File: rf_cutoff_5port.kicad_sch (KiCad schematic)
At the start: 11 parts

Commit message: Added mode switch
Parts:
- added SW?: SW_SP3T, symbol Switch:SW_SP3T
- J?: footprint (none) -> Connector_USB:USB_C_Receptacle_Amphenol_12401548E4-2A
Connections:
- net GND: now also SW?.4
- net at C?.1, Q?.3 (D), R?.1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: now also SW?.2; no longer Q?.2 (G)
- new net: Q?.2 (G), SW?.3
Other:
- note added: "RX AUTO"
- note added: "RX OFF"
- note added: "RX ON"
- moved on the sheet: C?, D?, J?, Q?, R?

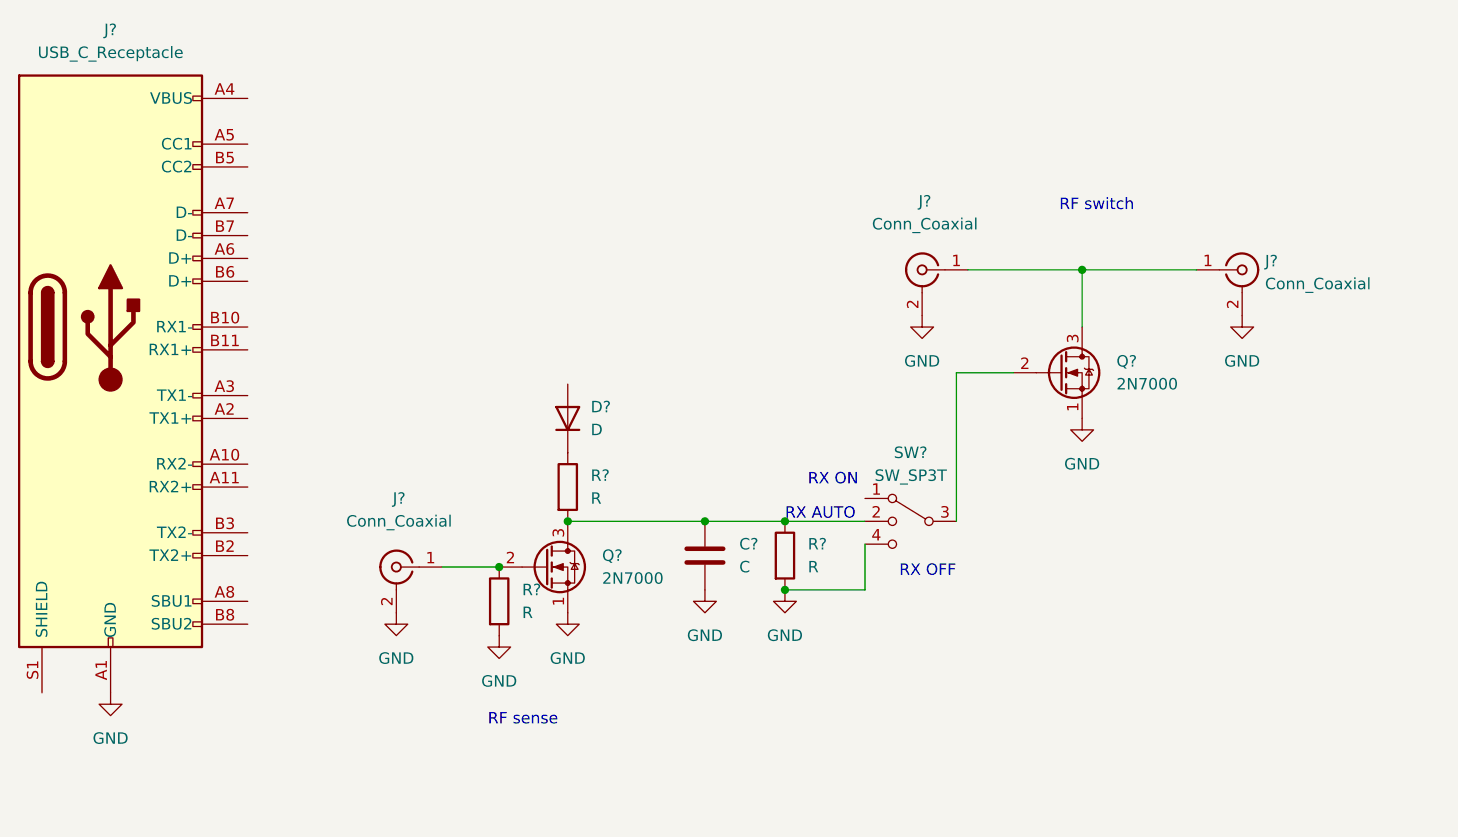
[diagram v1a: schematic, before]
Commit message: More wires including power
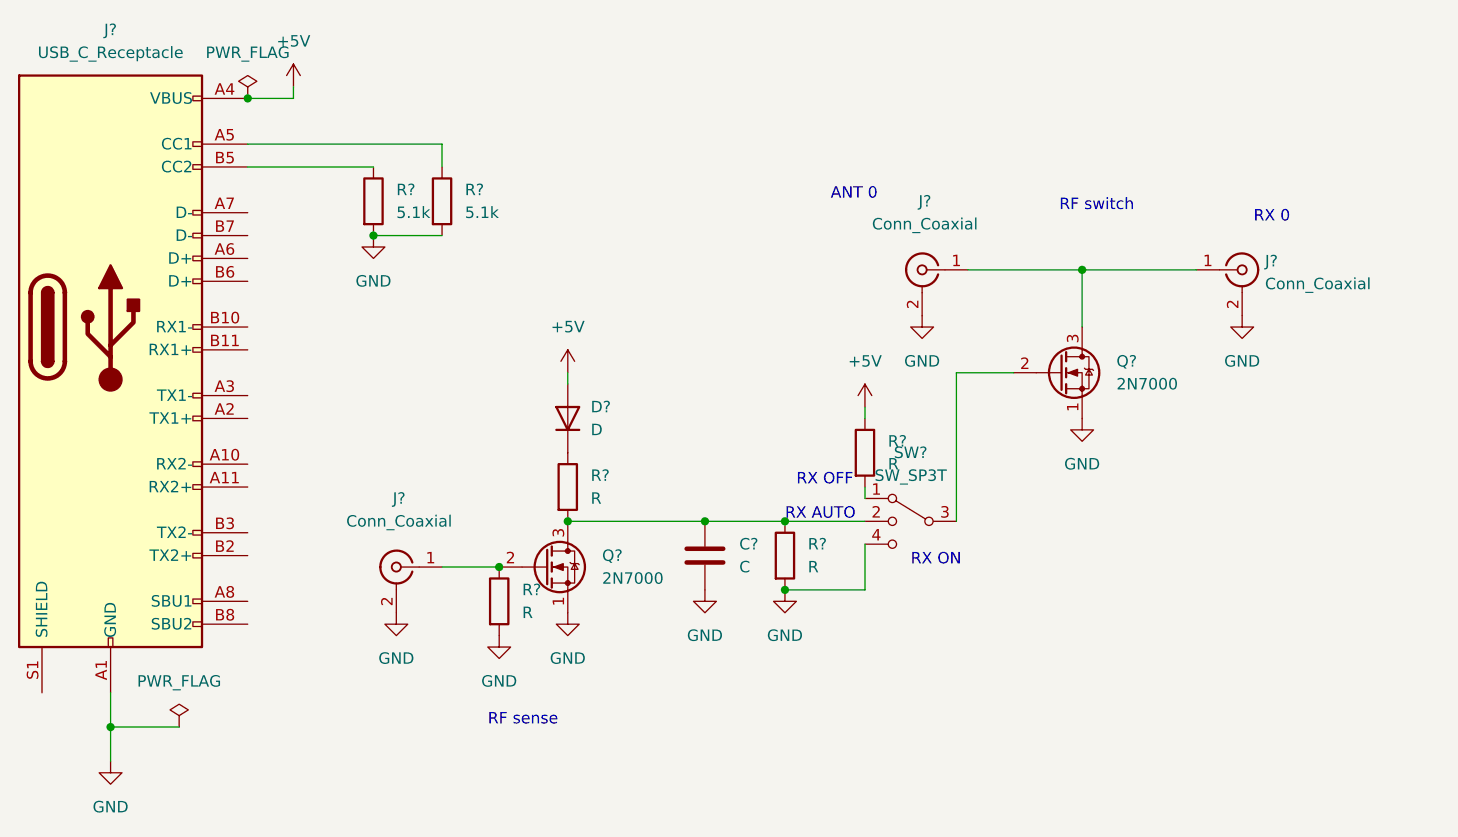
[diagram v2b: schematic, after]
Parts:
- added R? (x2): 5.1k, symbol Device:R
- added R?: R, symbol Device:R
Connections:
- net GND: now also R?.2, R?.2
- net at SW?.1: now also R?.2
- net +5V: now reaches D?.2 (A)
- net +5V: now also J?.A4 (VBUS), J?.A9 (VBUS), J?.B4 (VBUS), J?.B9 (VBUS), R?.1
- net at J?.A5 (CC1): now also R?.1
- net at J?.B5 (CC2): now also R?.1
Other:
- note added: "ANT 0"
- note added: "RX 0"

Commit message: Switched power supply to bias tee driven by RF port
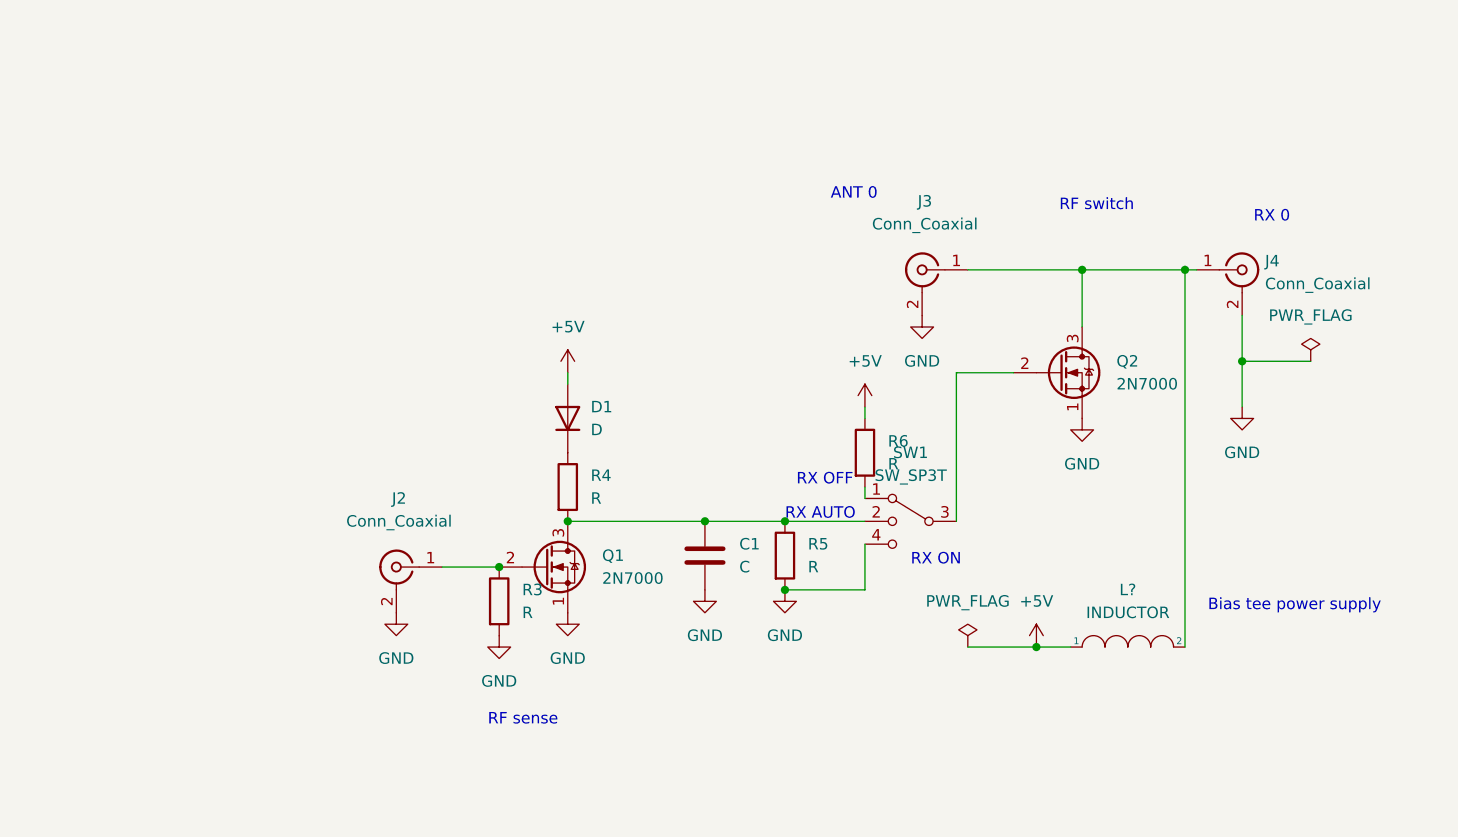
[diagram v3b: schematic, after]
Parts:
- removed J?: USB_C_Receptacle, Connector_USB:USB_C_Receptacle_Amphenol_12401548E4-2A, symbol Connector:USB_C_Receptacle
- removed R? (x2): 5.1k, symbol Device:R
- added L?: INDUCTOR, symbol pspice:INDUCTOR
- gave numbers to parts that had none: 12
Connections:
- net +5V: now also L?.1
- net at J3.1 (In), J4.1 (In), Q2.3 (D): now also L?.2
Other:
- note added: "Bias tee power supply"

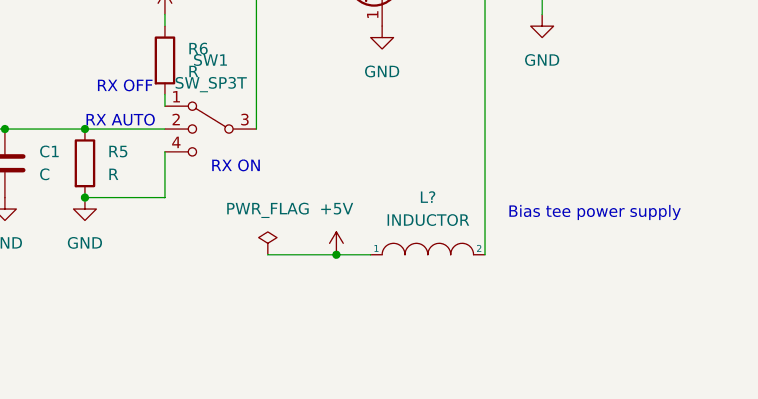
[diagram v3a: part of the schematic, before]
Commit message: Added filter capacitor to power supply
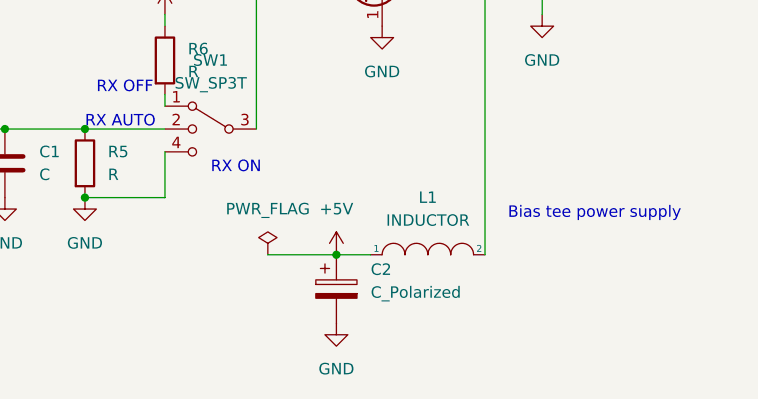
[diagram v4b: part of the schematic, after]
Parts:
- added C2: C_Polarized, symbol Device:C_Polarized
- gave numbers to parts that had none: 1
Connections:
- net +5V: now also C2.1
- net GND: now also C2.2
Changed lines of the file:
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@@
   (symbol (lib_id "pspice:INDUCTOR") (at 152.4 102.87 0) (unit 1)
     (in_bom yes) (on_board yes) (fields_autoplaced)
-    (property "Reference" "L?" (id 0) (at 152.4 96.52 0))
+    (property "Reference" "L1" (id 0) (at 152.4 96.52 0))
     (property "Value" "INDUCTOR" (id 1) (at 152.4 99.06 0))
     (property "Footprint" "" (id 2) (at 152.4 102.87 0)
@@
   (symbol (lib_id "power:+5V") (at 142.24 102.87 0) (unit 1)
     (in_bom yes) (on_board yes) (fields_autoplaced)
-    (property "Reference" "#PWR?" (id 0) (at 142.24 106.68 0)
+    (property "Reference" "#PWR01" (id 0) (at 142.24 106.68 0)
       (effects (font (size 1.27 1.27)) hide)
     )
@@
     (pin "3")
   )
+  (symbol (lib_id "Device:C_Polarized") (at 142.24 106.68 0) (unit 1)
+    (in_bom yes) (on_board yes) (fields_autoplaced)
+    (property "Reference" "C2" (id 0) (at 146.05 104.5209 0)
+      (effects (font (size 1.27 1.27)) (justify left))
+    )
+    (property "Value" "C_Polarized" (id 1) (at 146.05 107.0609 0)
+      (effects (font (size 1.27 1.27)) (justify left))
+    )
+    (property "Footprint" "" (id 2) (at 143.2052 110.49 0)
+      (effects (font (size 1.27 1.27)) hide)
+    )
+    (property "Datasheet" "~" (id 3) (at 142.24 106.68 0)
+      (effects (font (size 1.27 1.27)) hide)
+    )
+    (pin "1")
+    (pin "2")
+  )
   (symbol (lib_id "power:PWR_FLAG") (at 172.72 71.12 0) (unit 1)
     (in_bom yes) (on_board yes) (fields_autoplaced)
-    (property "Reference" "#FLG?" (id 0) (at 172.72 69.215 0)
+    (property "Reference" "#FLG02" (id 0) (at 172.72 69.215 0)
       (effects (font (size 1.27 1.27)) hide)
     )
@@
     (pin "1")
   )
+  (symbol (lib_id "power:GND") (at 142.24 110.49 0) (unit 1)
+    (in_bom yes) (on_board yes) (fields_autoplaced)
+    (property "Reference" "#PWR02" (id 0) (at 142.24 116.84 0)
+      (effects (font (size 1.27 1.27)) hide)
+    )
+    (property "Value" "GND" (id 1) (at 142.24 115.57 0))
+    (property "Footprint" "" (id 2) (at 142.24 110.49 0)
+      (effects (font (size 1.27 1.27)) hide)
+    )
+    (property "Datasheet" "" (id 3) (at 142.24 110.49 0)
+      (effects (font (size 1.27 1.27)) hide)
+    )
+    (pin "1")
+  )
   (symbol (lib_id "Device:R") (at 114.3 92.71 0) (unit 1)
     (in_bom yes) (on_board yes) (fields_autoplaced)
@@
   (symbol (lib_id "power:PWR_FLAG") (at 134.62 102.87 0) (unit 1)
     (in_bom yes) (on_board yes) (fields_autoplaced)
-    (property "Reference" "#FLG?" (id 0) (at 134.62 100.965 0)
+    (property "Reference" "#FLG01" (id 0) (at 134.62 100.965 0)
       (effects (font (size 1.27 1.27)) hide)
     )
@@
   )
   (symbol_instances
+    (path "/fdb0a8b1-189e-473a-a42a-8ded78934792"
+      (reference "#FLG01") (unit 1) (value "PWR_FLAG") (footprint "")
+    )
     (path "/b23f3c44-e488-41c2-92db-6ab908780acf"
-      (reference "#FLG?") (unit 1) (value "PWR_FLAG") (footprint "")
-    )
-    (path "/fdb0a8b1-189e-473a-a42a-8ded78934792"
-      (reference "#FLG?") (unit 1) (value "PWR_FLAG") (footprint "")
+      (reference "#FLG02") (unit 1) (value "PWR_FLAG") (footprint "")
+    )
+    (path "/9fbc8d26-048b-4e58-99b2-b3c2d2951708"
+      (reference "#PWR01") (unit 1) (value "+5V") (footprint "")
+    )
+    (path "/dcba9de9-5494-481d-8650-d561475d2ed5"
+      (reference "#PWR02") (unit 1) (value "GND") (footprint "")
     )
     (path "/0cf469a0-8efa-4786-aec4-457811b45978"
@@
       (reference "#PWR0113") (unit 1) (value "+5V") (footprint "")
     )
-    (path "/9fbc8d26-048b-4e58-99b2-b3c2d2951708"
-      (reference "#PWR?") (unit 1) (value "+5V") (footprint "")
-    )
     (path "/8b04b3db-6500-439f-91ea-1fa2bd402eb8"
       (reference "C1") (unit 1) (value "C") (footprint "")
     )
+    (path "/a4e46472-1e0e-4ade-8e38-0746fd677605"
+      (reference "C2") (unit 1) (value "C_Polarized") (footprint "")
+    )
     (path "/8c9b55d3-8f42-4a60-ad15-e45311b40479"
       (reference "D1") (unit 1) (value "D") (footprint "")
@@
     )
     (path "/2986eb5f-cd28-4a13-914f-db96c7e237c8"
-      (reference "L?") (unit 1) (value "INDUCTOR") (footprint "")
+      (reference "L1") (unit 1) (value "INDUCTOR") (footprint "")
     )
     (path "/a24a4b83-ff88-4faa-ab46-cc5a9eaa62f3"

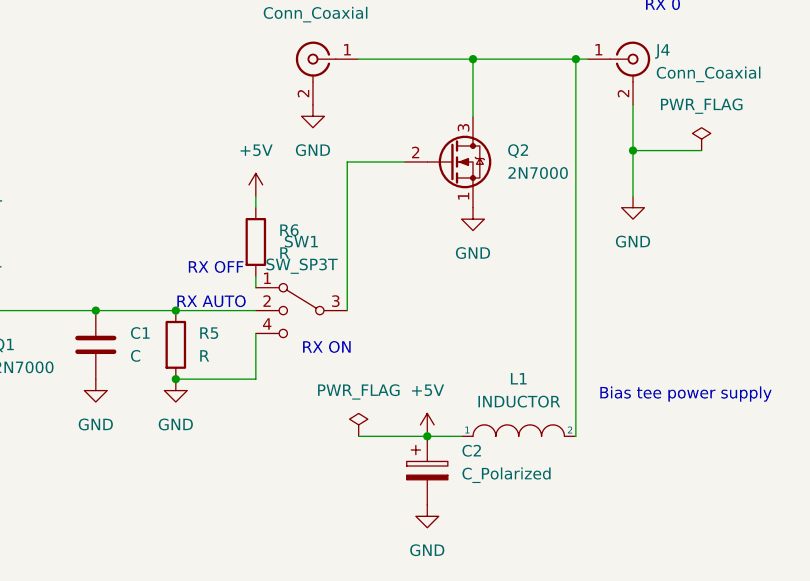
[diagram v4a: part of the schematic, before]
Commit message: Moved gate resistor
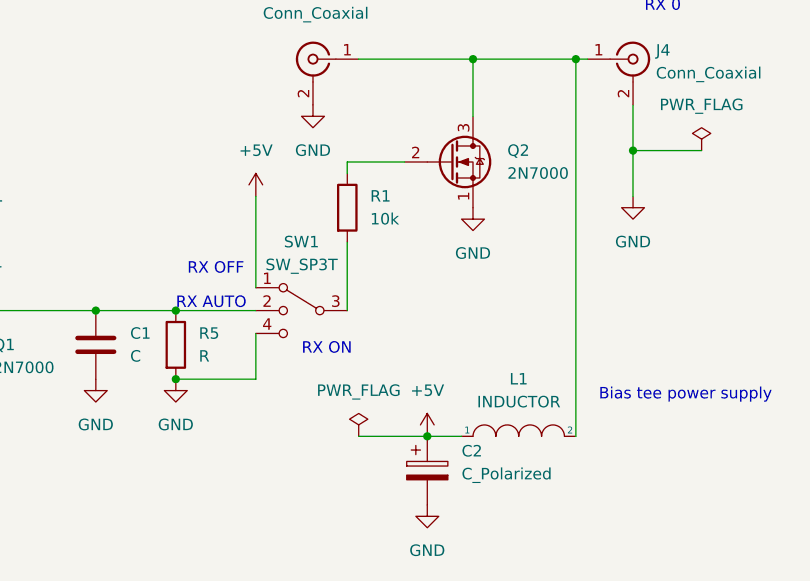
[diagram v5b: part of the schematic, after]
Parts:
- removed R6: R, symbol Device:R
- added R1: 10k, symbol Device:R
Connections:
- net +5V: now also SW1.1
- net at Q2.2 (G): now also R1.1; no longer SW1.3
- new net: R1.2, SW1.3
